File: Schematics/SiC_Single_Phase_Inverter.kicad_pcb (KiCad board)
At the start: 2 copper layers, 204.5 x 65.2 mm, 130 parts, among them IC1 F280049CPMSR, J1 23AH8786-Red, J10 464369202, J11 464379202, J12 43650-0418, J13 464369202, J14 464379202, J15 43650-0418, J16 464369202, J17 43650-0418, J18 43650-0418, J2 23AH8785-Black, J3 23AH8786-Red, J4 23AH8785-Black, J5 464379202, J6 464369202, J7 464379202, J8 464369202, J9 464379202, Q1 STB10NK60ZT4, Q2 C3M0025065K, Q3 C3M0025065K, Q4 C3M0025065K, Q5 C3M0025065K, Q6 STB10NK60ZT4, U1 UCC21710QDWRQ1, U2 UCC21710QDWRQ1, U3 UCC21710QDWRQ1, U4 UCC21710QDWRQ1, U5 TR05S3V3

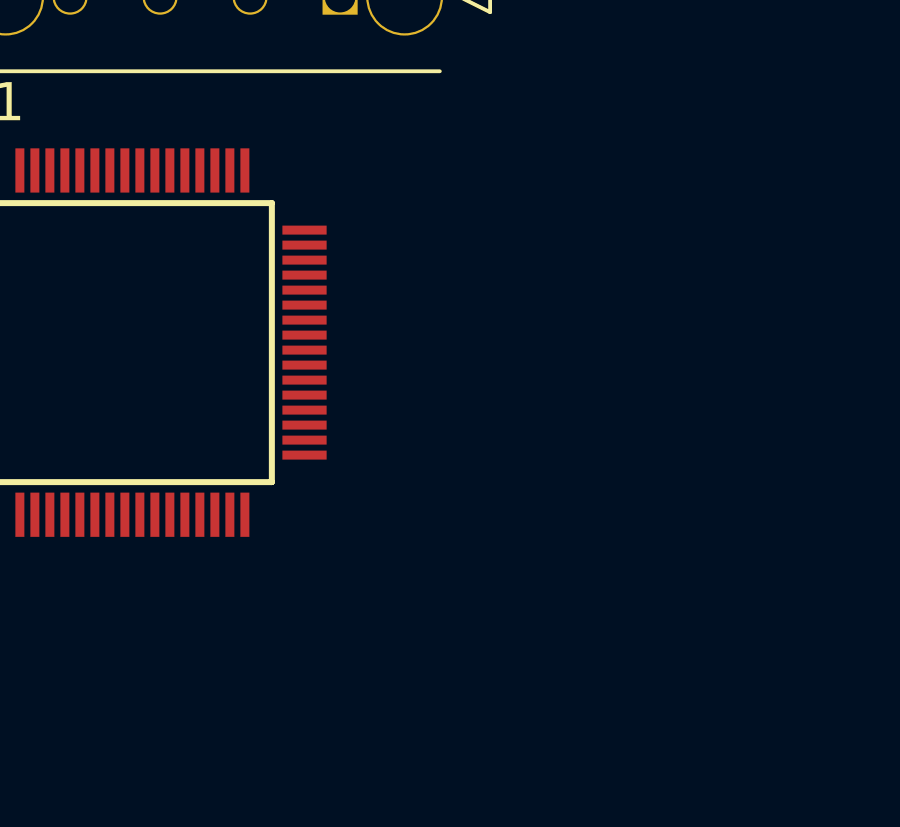
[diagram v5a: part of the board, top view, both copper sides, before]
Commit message: WIP: Work on Controller layout, and fixed some sheet text and positions
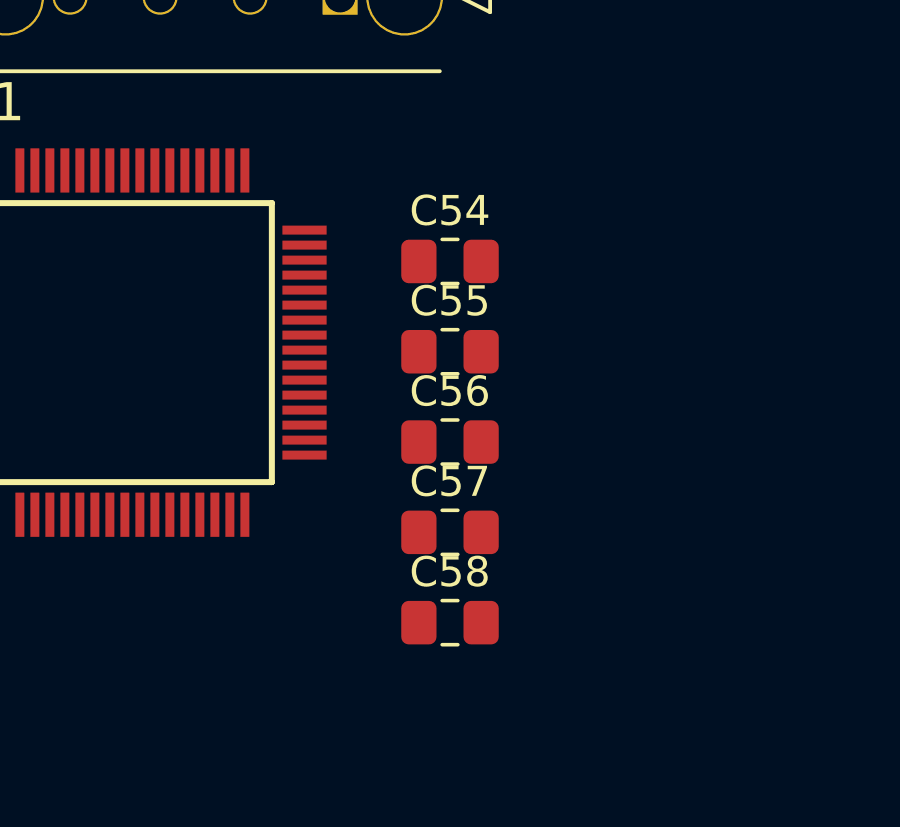
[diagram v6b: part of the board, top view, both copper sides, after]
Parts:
- added C54: 0.1 uF, Capacitor_SMD:C_0805_2012Metric_Pad1.18x1.45mm_HandSolder, F.Cu at (470.5, 184.0)
- added C55: 0.1 uF, Capacitor_SMD:C_0805_2012Metric_Pad1.18x1.45mm_HandSolder, F.Cu at (470.5, 187.0)
- added C56: 0.1 uF, Capacitor_SMD:C_0805_2012Metric_Pad1.18x1.45mm_HandSolder, F.Cu at (470.5, 190.0)
- added C57: 0.1 uF, Capacitor_SMD:C_0805_2012Metric_Pad1.18x1.45mm_HandSolder, F.Cu at (470.5, 193.0)
- added C58: 10 uF, Capacitor_SMD:C_0805_2012Metric_Pad1.18x1.45mm_HandSolder, F.Cu at (470.5, 196.0)
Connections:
- IC1 pad 21: unconnected-(IC1-VSSA-Pad21) -> LOGIC_GND
- IC1 pad 22: unconnected-(IC1-VDDA-Pad22) -> +3V3
- IC1 pad 26: unconnected-(IC1-VSS_2-Pad26) -> LOGIC_GND
- IC1 pad 27: unconnected-(IC1-VDD_2-Pad27) -> +3V3
- IC1 pad 4: unconnected-(IC1-VDD_1-Pad4) -> +3V3
- IC1 pad 44: unconnected-(IC1-VDD_3-Pad44) -> +3V3
- IC1 pad 45: unconnected-(IC1-VSS_3-Pad45) -> LOGIC_GND
- IC1 pad 49: unconnected-(IC1-GPIO3-Pad49) -> /Controller/ePWM_B_L
- IC1 pad 5: unconnected-(IC1-VSS_1-Pad5) -> LOGIC_GND
- IC1 pad 50: unconnected-(IC1-GPIO2-Pad50) -> /Controller/ePWM_B_H
- IC1 pad 51: unconnected-(IC1-GPIO1-Pad51) -> /Controller/ePWM_A_L
- IC1 pad 52: unconnected-(IC1-GPIO0-Pad52) -> /Controller/ePWM_A_H
- IC1 pad 58: unconnected-(IC1-VSS_4-Pad58) -> LOGIC_GND
- IC1 pad 59: unconnected-(IC1-VDD_4-Pad59) -> +3V3
- J18 pad 2: +15V_ISO_LALS -> +15V_ISO_LBLS
- J18 pad 4: +15V_ISO_LALS -> +15V_ISO_LBLS
- PS1 pad 16: +15V_ISO_LALS -> +15V_ISO_LBLS
- PS2 pad 16: +15V_ISO_LALS -> +15V_ISO_LBLS
- U5 pad 1: +15V_ISO_LALS -> +15V_ISO_LBLS

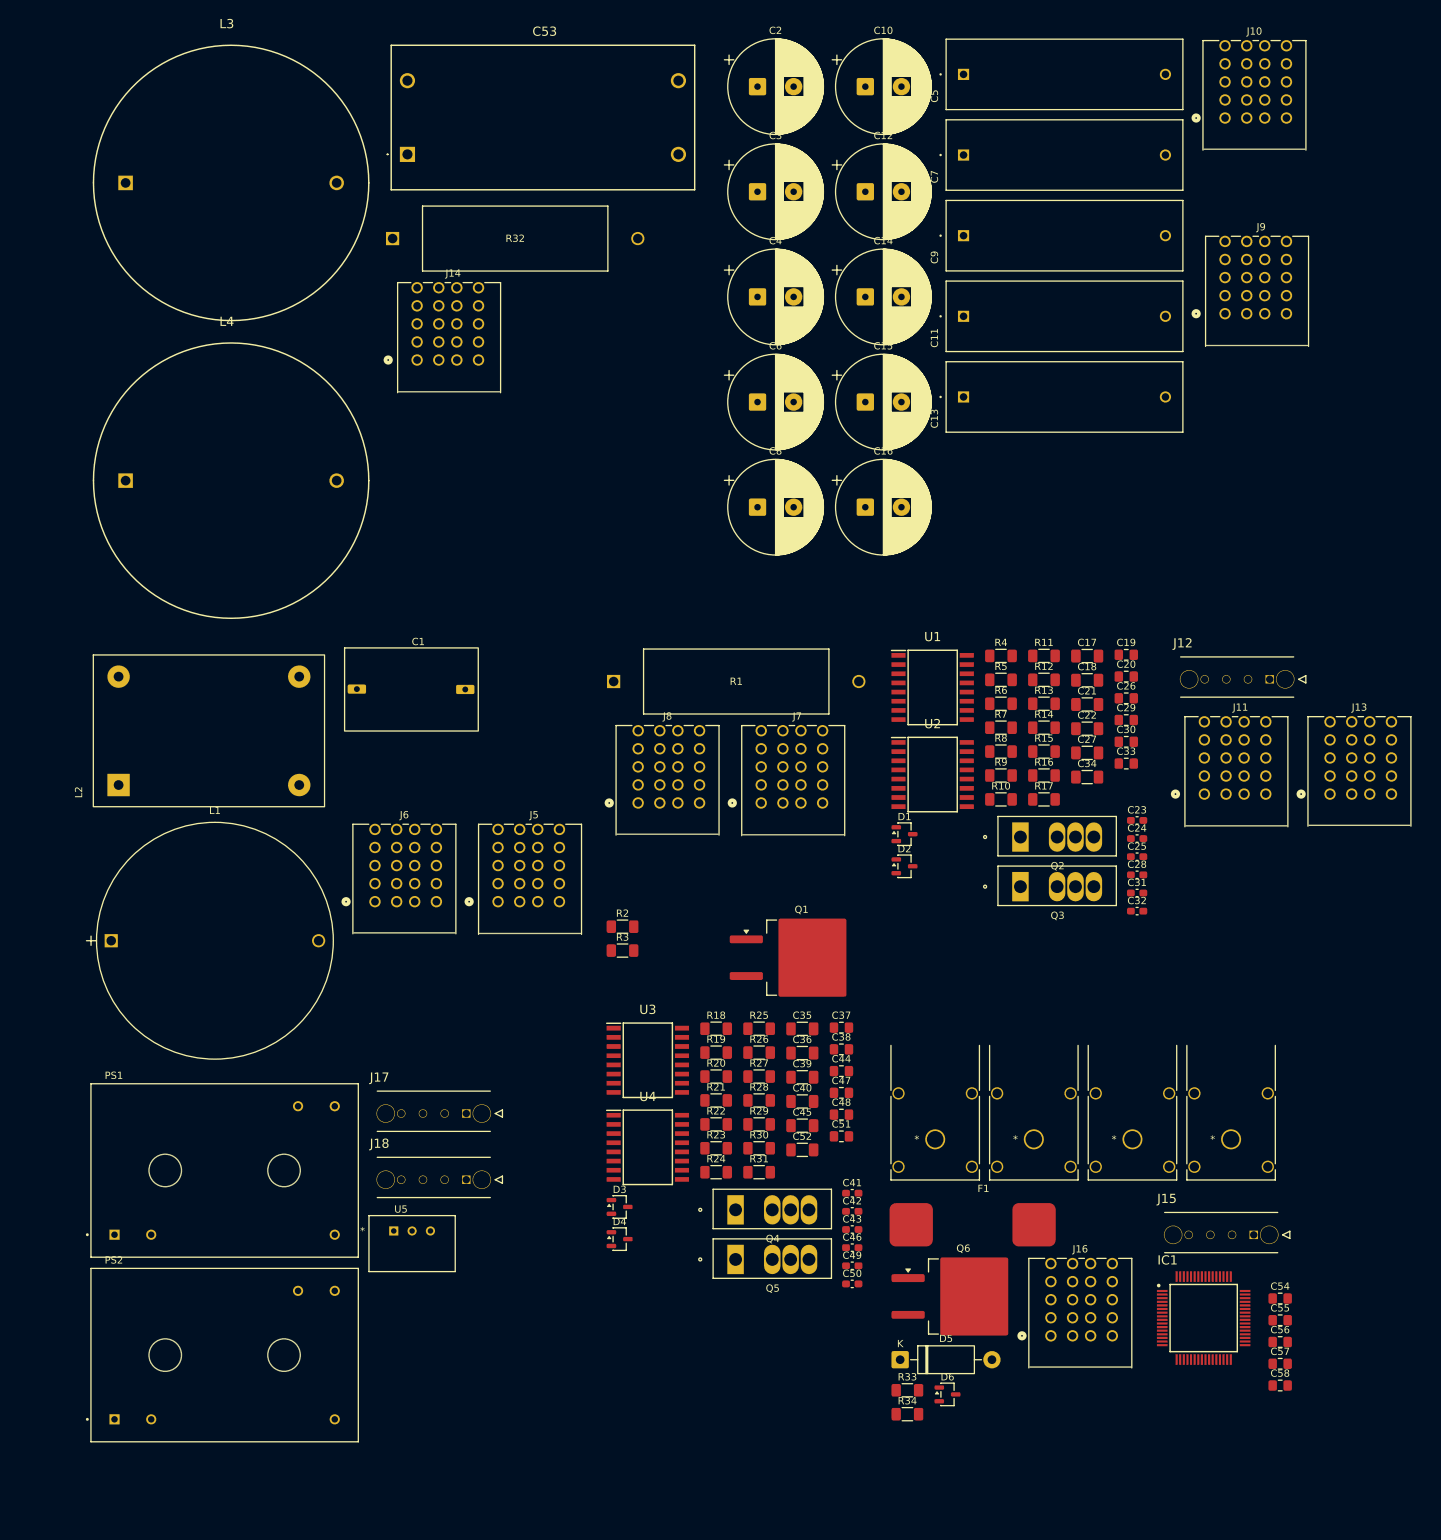
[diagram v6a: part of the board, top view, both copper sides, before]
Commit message: [WIP Controller Design]
- Wired up all 64 Pins on the Controller
- Added 3d models for connectors and Controller
- Added data sheets for the newly added parts
- wired connectors to controller to external PCB Boards
- Updated Text fields
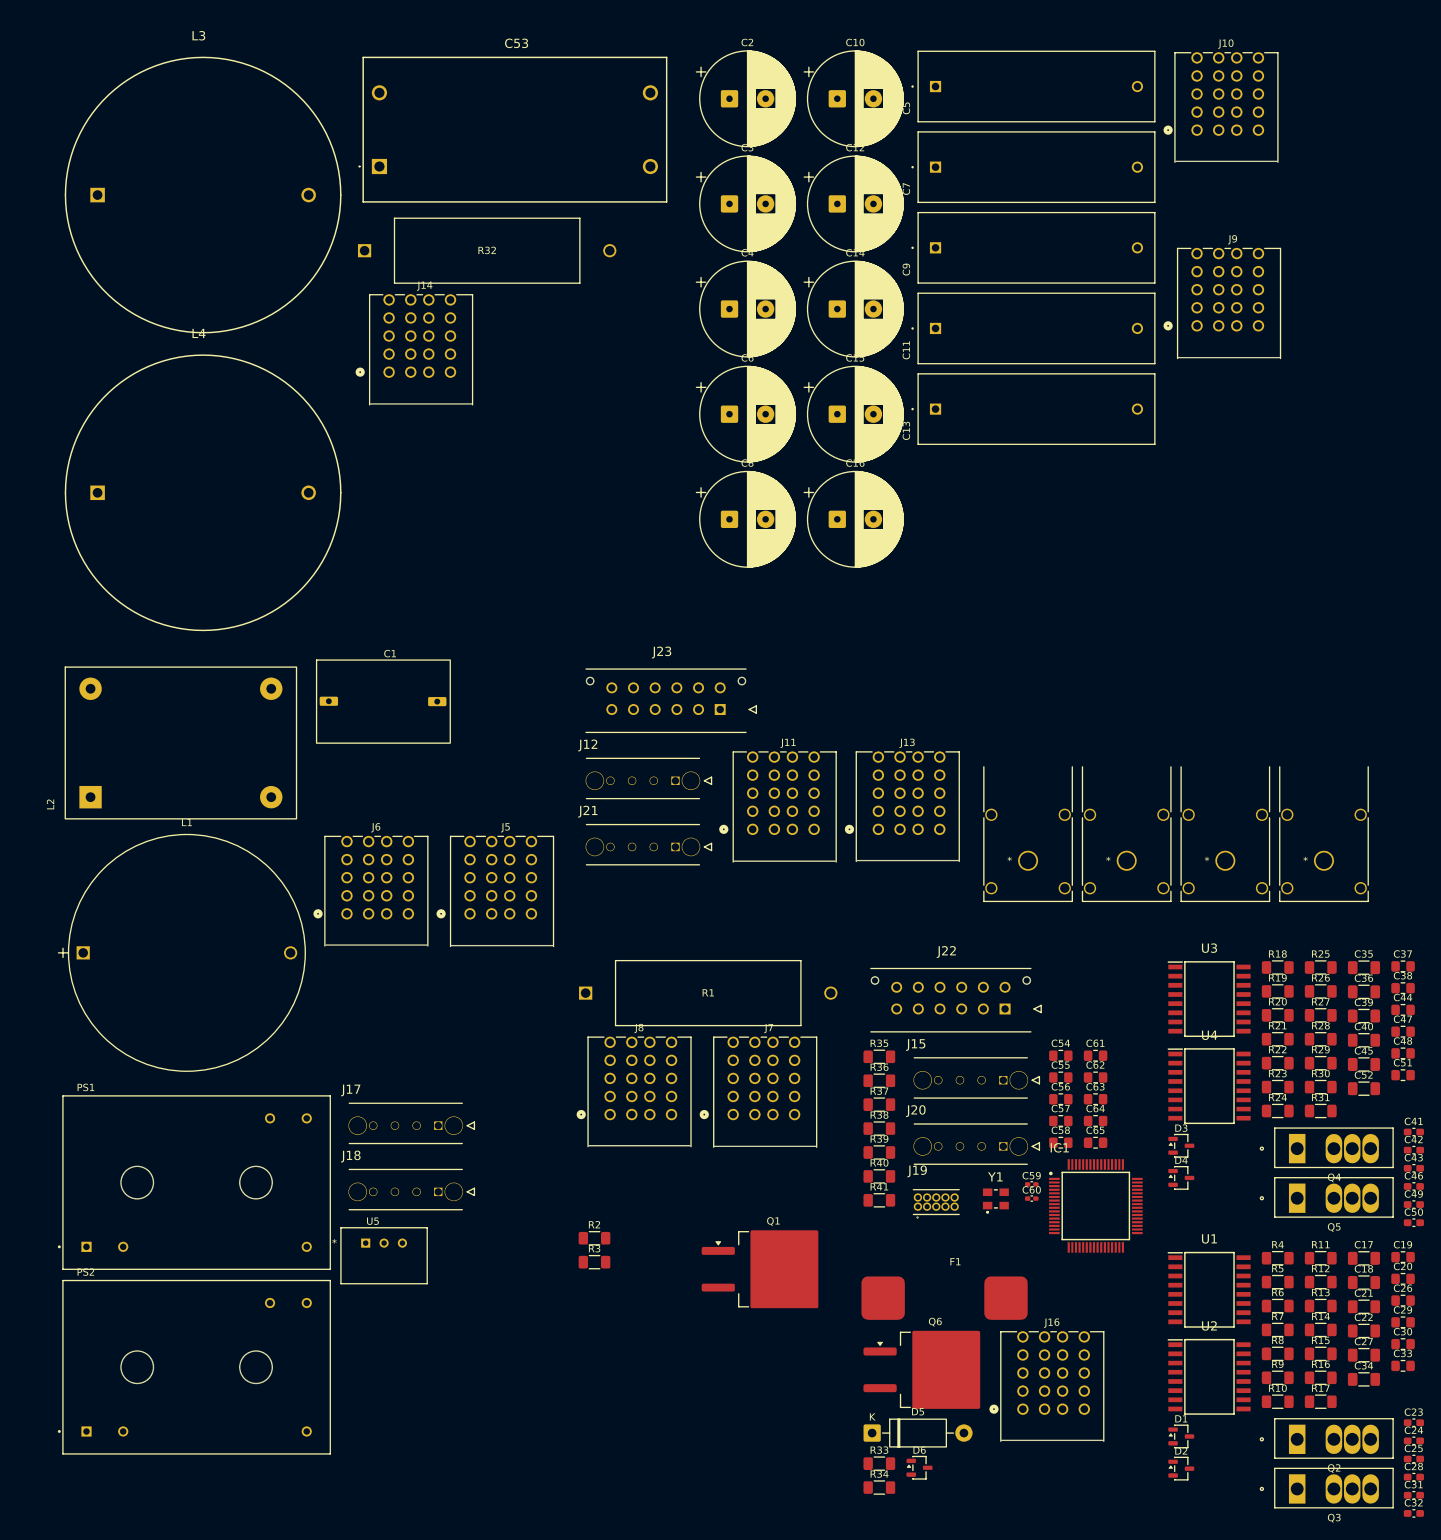
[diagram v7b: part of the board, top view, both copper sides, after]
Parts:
- added C59: 18 pF, Capacitor_SMD:C_0402_1005Metric_Pad0.74x0.62mm_HandSolder, F.Cu at (436.1, 168.2)
- added C60: 18 pF, Capacitor_SMD:C_0402_1005Metric_Pad0.74x0.62mm_HandSolder, F.Cu at (436.1, 170.1)
- added C61: 0.1 uF, Capacitor_SMD:C_0805_2012Metric_Pad1.18x1.45mm_HandSolder, F.Cu at (444.9, 150.4)
- added C62: 0.1 uF, Capacitor_SMD:C_0805_2012Metric_Pad1.18x1.45mm_HandSolder, F.Cu at (444.9, 153.4)
- added C63: 0.1 uF, Capacitor_SMD:C_0805_2012Metric_Pad1.18x1.45mm_HandSolder, F.Cu at (444.9, 156.4)
- added C64: 0.1 uF, Capacitor_SMD:C_0805_2012Metric_Pad1.18x1.45mm_HandSolder, F.Cu at (444.9, 159.4)
- added C65: 0.1 uF, Capacitor_SMD:C_0805_2012Metric_Pad1.18x1.45mm_HandSolder, F.Cu at (444.9, 162.4)
- added J19: FTSH-105-01-LM-D-K, SiC_Inverter:FTSH-105-01-LM-D-K, F.Cu at (420.3, 171.2)
- added J20: 43650-0418, SiC_Inverter:436500418, F.Cu at (432.1, 162.9)
- added J21: 43650-0418, SiC_Inverter:436500418, F.Cu at (386.8, 121.5)
- added J22: 43045-1212, SiC_Inverter:43045-1212, F.Cu at (432.4, 143.9)
- added J23: 43045-1212, SiC_Inverter:43045-1212, F.Cu at (393.0, 102.5)
- added R35: 100K, Resistor_SMD:R_1206_3216Metric_Pad1.30x1.75mm_HandSolder, F.Cu at (415.0, 150.5)
- added R36: 100K, Resistor_SMD:R_1206_3216Metric_Pad1.30x1.75mm_HandSolder, F.Cu at (415.0, 153.8)
- added R37: 100K, Resistor_SMD:R_1206_3216Metric_Pad1.30x1.75mm_HandSolder, F.Cu at (415.0, 157.1)
- added R38: 100K, Resistor_SMD:R_1206_3216Metric_Pad1.30x1.75mm_HandSolder, F.Cu at (415.0, 160.4)
- added R39: 100K, Resistor_SMD:R_1206_3216Metric_Pad1.30x1.75mm_HandSolder, F.Cu at (415.0, 163.8)
- added R40: 100K, Resistor_SMD:R_1206_3216Metric_Pad1.30x1.75mm_HandSolder, F.Cu at (415.0, 167.1)
- added R41: 100K, Resistor_SMD:R_1206_3216Metric_Pad1.30x1.75mm_HandSolder, F.Cu at (415.0, 170.4)
- added Y1: ABM8-20.000MHZ-B2-T, SiC_Inverter:ABM8-20.000MHZ-B2-T, F.Cu at (431.1, 170.2)
- R10, R12, R13, R15, R16, R17, R24, R26, R27, R29, R30, R31: value 5K -> 5 K
- moved C17 91.7 mm to (482.1, 178.4)
- moved C18 91.7 mm to (482.1, 181.8)
- moved C21 91.7 mm to (482.1, 185.1)
- moved C22 91.7 mm to (482.1, 188.4)
- moved C27 91.7 mm to (482.1, 191.8)
- moved C34 91.7 mm to (482.1, 195.2)
- moved Q2 91.7 mm to (472.8, 203.4)
- moved Q3 91.7 mm to (472.8, 210.3)
- moved R10 91.7 mm to (470.1, 198.2)
- moved R11 91.7 mm to (476.1, 178.4)
- moved R12 91.7 mm to (476.1, 181.7)
- moved R13 91.7 mm to (476.1, 185.0)
- moved R14 91.7 mm to (476.1, 188.3)
- moved R15 91.7 mm to (476.1, 191.6)
- moved R16 91.7 mm to (476.1, 194.9)
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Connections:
- C23 pad 1: /Full-Bridge/LS_LegA_RDY -> /Con_RDY_A_L
- C24 pad 1: /Full-Bridge/~{LS_LegA_FLT} -> /Con_FLT_A_L
- C25 pad 1: /Full-Bridge/LS_LegA_EN -> /Con_EN_A_L
- C28 pad 1: /Full-Bridge/HS_LegA_RDY -> /Con_RDY_A_H
- C31 pad 1: /Full-Bridge/~{HS_LegA_FLT} -> /Con_FLT_A_H
- C32 pad 1: /Full-Bridge/HS_LegA_EN -> /Con_EN_A_H
- C41 pad 1: /Full-Bridge/LS_LegB_RDY -> /Con_RDY_B_L
- C42 pad 1: /Full-Bridge/~{LS_LegB_FLT} -> /Con_FLT_B_L
- C43 pad 1: /Full-Bridge/LS_LegB_EN -> /Con_EN_B_L
- C46 pad 1: /Full-Bridge/HS_LegB_RDY -> /Con_RDY_B_H
- C49 pad 1: /Full-Bridge/~{HS_LegB_FLT} -> /Con_FLT_B_H
- C50 pad 1: /Full-Bridge/HS_LegB_EN -> /Con_EN_B_H
- IC1 pad 1: unconnected-(IC1-GPIO29-Pad1) -> /Controller/SCIRXDA
- IC1 pad 10: unconnected-(IC1-PGA1_GNDPGA3_GNDPGA5_GND-Pad10) -> LOGIC_GND
- IC1 pad 14: unconnected-(IC1-A1DACB_OUT-Pad14) -> /Controller/VOUT_Sense
- IC1 pad 15: unconnected-(IC1-A0B15C15DACA_OUT-Pad15) -> /Controller/DCBUS_Sense
- IC1 pad 16: unconnected-(IC1-VREFHIAVREFHIBVREFHIC-Pad16) -> +3V3
- IC1 pad 17: unconnected-(IC1-VREFLOAVREFLOBVREFLOC-Pad17) -> LOGIC_GND
- IC1 pad 2: unconnected-(IC1-GPIO28-Pad2) -> /Controller/SCITXDA
- IC1 pad 20: unconnected-(IC1-PGA2_GNDPGA4_GNDPGA6_GND-Pad20) -> LOGIC_GND
- IC1 pad 25: unconnected-(IC1-A10B1C10PGA7_OF-Pad25) -> /Controller/I_OUT_A_Sense
- IC1 pad 28: unconnected-(IC1-VDDIO_1-Pad28) -> +3V3
- IC1 pad 29: unconnected-(IC1-GPIO13-Pad29) -> /Con_RDY_A_L
- IC1 pad 3: unconnected-(IC1-XRSN-Pad3) -> /Controller/XRSn
- IC1 pad 30: unconnected-(IC1-GPIO12-Pad30) -> /Con_RDY_A_H
- IC1 pad 31: unconnected-(IC1-GPIO11-Pad31) -> /Con_FLT_B_L
- IC1 pad 33: unconnected-(IC1-GPIO16-Pad33) -> /Con_RDY_B_L
- IC1 pad 34: unconnected-(IC1-GPIO17-Pad34) -> /Con_RDY_B_H
- IC1 pad 35: unconnected-(IC1-GPIO24-Pad35) -> /Controller/Flash_Boot_PU
- IC1 pad 36: unconnected-(IC1-TCK-Pad36) -> /Controller/TCK
- IC1 pad 37: unconnected-(IC1-GPIO37/TDO-Pad37) -> /Controller/TDO
- IC1 pad 38: unconnected-(IC1-TMS-Pad38) -> /Controller/TMS
- IC1 pad 39: unconnected-(IC1-GPIO35/TDI-Pad39) -> /Controller/TDI
- IC1 pad 40: unconnected-(IC1-GPIO32-Pad40) -> /Controller/Flash_Boot_PD
- IC1 pad 41: unconnected-(IC1-GPIO18_X2-Pad41) -> /Controller/X2
- IC1 pad 42: unconnected-(IC1-X1-Pad42) -> /Controller/X1
- IC1 pad 43: unconnected-(IC1-VDDIO_2-Pad43) -> +3V3
- IC1 pad 46: unconnected-(IC1-VREGENZ-Pad46) -> LOGIC_GND
- IC1 pad 47: unconnected-(IC1-GPIO8-Pad47) -> /Con_FLT_A_H
- IC1 pad 48: unconnected-(IC1-GPIO4-Pad48) -> /Con_EN_A_H
- IC1 pad 49: /Controller/ePWM_B_L -> /Con_PWM_B_L
- IC1 pad 50: /Controller/ePWM_B_H -> /Con_PWM_B_H
- IC1 pad 51: /Controller/ePWM_A_L -> /Con_PWM_A_L
- IC1 pad 52: /Controller/ePWM_A_H -> /Con_PWM_A_H
- IC1 pad 53: unconnected-(IC1-VDDIO_SW-Pad53) -> +3V3
- IC1 pad 55: unconnected-(IC1-VSS_SW-Pad55) -> LOGIC_GND
- IC1 pad 57: unconnected-(IC1-GPIO7-Pad57) -> /Con_EN_B_L
- IC1 pad 60: unconnected-(IC1-VDDIO_3-Pad60) -> +3V3
- IC1 pad 61: unconnected-(IC1-GPIO5-Pad61) -> /Con_EN_A_L
- IC1 pad 62: unconnected-(IC1-GPIO9-Pad62) -> /Con_FLT_A_L
- IC1 pad 63: unconnected-(IC1-GPIO10-Pad63) -> /Con_FLT_B_H
- IC1 pad 64: unconnected-(IC1-GPIO6-Pad64) -> /Con_EN_B_H
- IC1 pad 7: unconnected-(IC1-B2C6PGA3_OF-Pad7) -> /Controller/I_OUT_B_Sense
- R10 pad 2: /Full-Bridge/LS_LegA_EN -> /Con_EN_A_L
- R11 pad 2: /Full-Bridge/PWM_A_L -> /Con_PWM_A_L
- R12 pad 2: /Full-Bridge/HS_LegA_EN -> /Con_EN_A_H
- R13 pad 2: /Full-Bridge/~{LS_LegA_FLT} -> /Con_FLT_A_L
- R14 pad 2: /Full-Bridge/PWM_A_H -> /Con_PWM_A_H
- R15 pad 2: /Full-Bridge/~{HS_LegA_FLT} -> /Con_FLT_A_H
- R16 pad 2: /Full-Bridge/LS_LegA_RDY -> /Con_RDY_A_L
- R17 pad 2: /Full-Bridge/HS_LegA_RDY -> /Con_RDY_A_H
- R24 pad 2: /Full-Bridge/LS_LegB_EN -> /Con_EN_B_L
- R25 pad 2: /Full-Bridge/PWM_B_L -> /Con_PWM_B_L
- R26 pad 2: /Full-Bridge/HS_LegB_EN -> /Con_EN_B_H
- R27 pad 2: /Full-Bridge/~{LS_LegB_FLT} -> /Con_FLT_B_L
- R28 pad 2: /Full-Bridge/PWM_B_H -> /Con_PWM_B_H
- R29 pad 2: /Full-Bridge/~{HS_LegB_FLT} -> /Con_FLT_B_H
- R30 pad 2: /Full-Bridge/LS_LegB_RDY -> /Con_RDY_B_L
- R31 pad 2: /Full-Bridge/HS_LegB_RDY -> /Con_RDY_B_H
- U1 pad 12: /Full-Bridge/LS_LegA_RDY -> /Con_RDY_A_L
- U1 pad 13: /Full-Bridge/~{LS_LegA_FLT} -> /Con_FLT_A_L
- U1 pad 14: /Full-Bridge/LS_LegA_EN -> /Con_EN_A_L
- U2 pad 12: /Full-Bridge/HS_LegA_RDY -> /Con_RDY_A_H
- U2 pad 13: /Full-Bridge/~{HS_LegA_FLT} -> /Con_FLT_A_H
- U2 pad 14: /Full-Bridge/HS_LegA_EN -> /Con_EN_A_H
- U3 pad 12: /Full-Bridge/LS_LegB_RDY -> /Con_RDY_B_L
- U3 pad 13: /Full-Bridge/~{LS_LegB_FLT} -> /Con_FLT_B_L
- U3 pad 14: /Full-Bridge/LS_LegB_EN -> /Con_EN_B_L
- U4 pad 12: /Full-Bridge/HS_LegB_RDY -> /Con_RDY_B_H
- U4 pad 13: /Full-Bridge/~{HS_LegB_FLT} -> /Con_FLT_B_H
- U4 pad 14: /Full-Bridge/HS_LegB_EN -> /Con_EN_B_H
